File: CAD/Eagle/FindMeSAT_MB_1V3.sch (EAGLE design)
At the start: 136 parts, among them Q101 ABS07-32.768KHZ, Q651 ABM3B-16MHZ-10-R50-1-U, U1001 CFPT-141-20MHZ, U101 ATXMEGA256A3BU-AU, U1011 OPA354, U1021 OPA354, U1111 LM2831YMF, U1121 LM4120IM5-3.0, U201 SIM808, U301 MPU-9250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

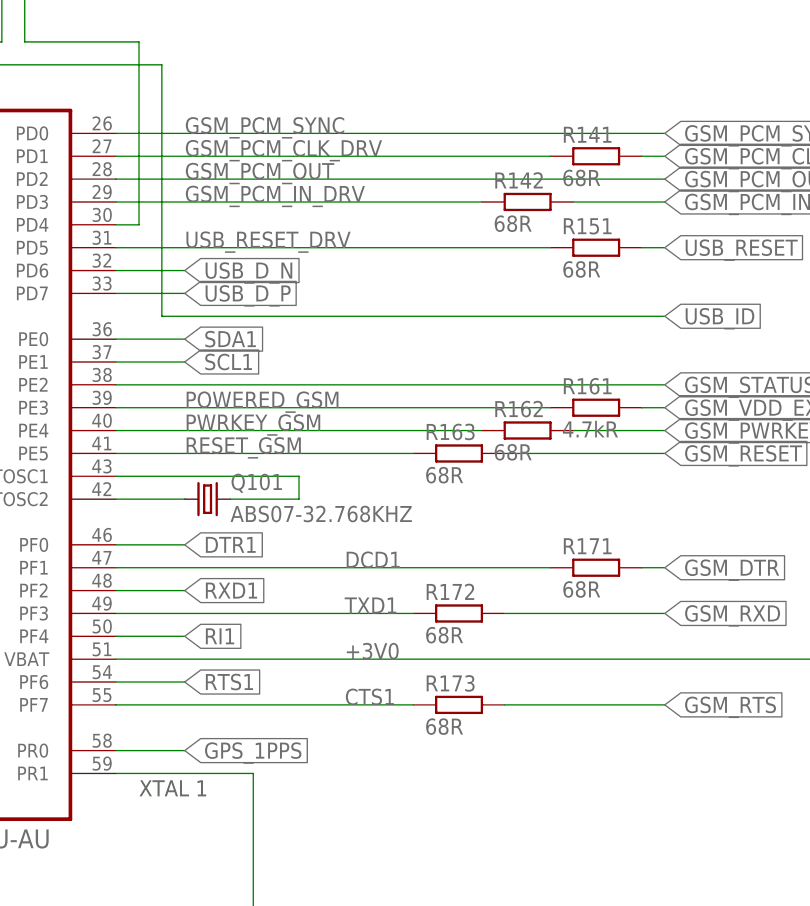
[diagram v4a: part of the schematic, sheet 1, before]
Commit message: HW_V1.3 - Polyfuse of USB - value changed from 0.5A/1.0A to 1.1A/2.2A - some net names fixed
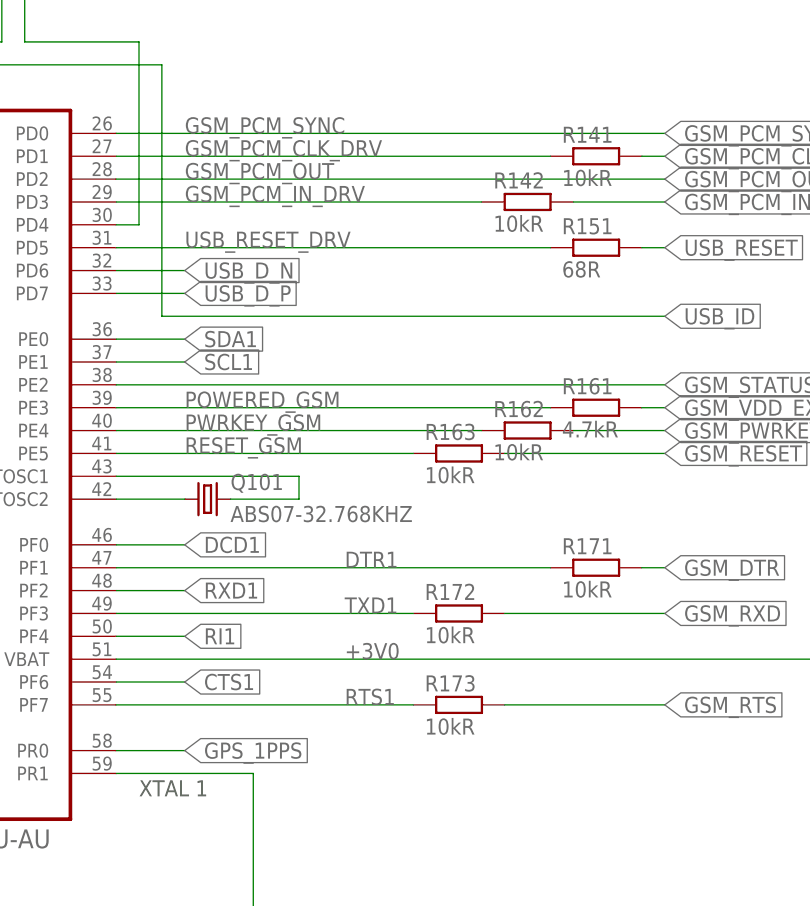
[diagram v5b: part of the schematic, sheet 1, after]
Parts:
- R141, R142, R162, R163, R171, R172, R173: value 68R -> 10kR
- RPOLY711: value 0.5A/1.0A -> 1.1A/2.2A
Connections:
- net CTS1: now also R223.1, U101A.PF6; no longer R173.1, U101A.PF7
- net DCD1: now also R222.1, U101A.PF0; no longer R171.1, U101A.PF1
- net DTR1: now also R171.1, U101A.PF1; no longer R222.1, U101A.PF0
- net RTS1: now also R173.1, U101A.PF7; no longer R223.1, U101A.PF6
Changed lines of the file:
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@@
 <part name="GND1203" library="df4iah_supply" deviceset="GND" device=""/>
 <part name="GND701" library="df4iah_supply" deviceset="GND" device=""/>
-<part name="RPOLY711" library="rcl" deviceset="R-EU_" device="M1206" value="0.5A/1.0A"/>
+<part name="RPOLY711" library="rcl" deviceset="R-EU_" device="M1206" value="1.1A/2.2A"/>
 <part name="R722" library="rcl" deviceset="R-EU_" device="R0603" value="68R"/>
 <part name="R723" library="rcl" deviceset="R-EU_" device="R0603" value="68R"/>
@@
 <part name="R212" library="rcl" deviceset="R-EU_" device="R0603" value="10kR"/>
 <part name="+3V3_211" library="df4iah_supply" deviceset="+3V3" device=""/>
-<part name="R172" library="rcl" deviceset="R-EU_" device="R0603" value="68R"/>
+<part name="R172" library="rcl" deviceset="R-EU_" device="R0603" value="10kR"/>
 <part name="R224" library="rcl" deviceset="R-EU_" device="R0603" value="68R"/>
 <part name="R223" library="rcl" deviceset="R-EU_" device="R0603" value="68R"/>
 <part name="R221" library="rcl" deviceset="R-EU_" device="R0603" value="68R"/>
-<part name="R173" library="rcl" deviceset="R-EU_" device="R0603" value="68R"/>
-<part name="R171" library="rcl" deviceset="R-EU_" device="R0603" value="68R"/>
+<part name="R173" library="rcl" deviceset="R-EU_" device="R0603" value="10kR"/>
+<part name="R171" library="rcl" deviceset="R-EU_" device="R0603" value="10kR"/>
 <part name="R222" library="rcl" deviceset="R-EU_" device="R0603" value="68R"/>
 <part name="R271" library="rcl" deviceset="R-EU_" device="R0805"/>
@@
 <part name="C251" library="rcl" deviceset="C-EU" device="C0603" value="100pF"/>
 <part name="GND231" library="df4iah_supply" deviceset="GND" device=""/>
-<part name="R163" library="rcl" deviceset="R-EU_" device="R0603" value="68R"/>
-<part name="R162" library="rcl" deviceset="R-EU_" device="R0603" value="68R"/>
+<part name="R163" library="rcl" deviceset="R-EU_" device="R0603" value="10kR"/>
+<part name="R162" library="rcl" deviceset="R-EU_" device="R0603" value="10kR"/>
 <part name="R161" library="rcl" deviceset="R-EU_" device="R0603" value="4.7kR"/>
 <part name="R231" library="rcl" deviceset="R-EU_" device="R0603" value="68R"/>
@@
 <part name="R234" library="rcl" deviceset="R-EU_" device="R0603" value="68R"/>
 <part name="R241" library="rcl" deviceset="R-EU_" device="R0603" value="68R"/>
-<part name="R141" library="rcl" deviceset="R-EU_" device="R0603" value="68R"/>
-<part name="R142" library="rcl" deviceset="R-EU_" device="R0603" value="68R"/>
+<part name="R141" library="rcl" deviceset="R-EU_" device="R0603" value="10kR"/>
+<part name="R142" library="rcl" deviceset="R-EU_" device="R0603" value="10kR"/>
 <part name="+3V3_121" library="df4iah_supply" deviceset="+3V3" device=""/>
 <part name="R251" library="rcl" deviceset="R-EU_" device="R0603" value="68R"/>
@@
 </segment>
 </net>
-<net name="RTS1" class="0">
+<net name="CTS1" class="0">
 <segment>
 <pinref part="U101" gate="A" pin="PF6"/>
@@
 </segment>
 </net>
-<net name="CTS1" class="0">
+<net name="RTS1" class="0">
 <segment>
 <pinref part="U101" gate="A" pin="PF7"/>
@@
 </segment>
 </net>
-<net name="DCD1" class="0">
+<net name="DTR1" class="0">
 <segment>
 <pinref part="R171" gate="G$1" pin="1"/>
@@
 </segment>
 </net>
-<net name="DTR1" class="0">
+<net name="DCD1" class="0">
 <segment>
 <pinref part="U101" gate="A" pin="PF0"/>
@@
 </segment>
 </net>
-<net name="RTS1" class="0">
-<segment>
-<pinref part="R223" gate="G$1" pin="1"/>
-<wire x1="86.36" y1="152.4" x2="33.02" y2="152.4" width="0.1524" layer="91"/>
-<label x="33.02" y="152.4" size="1.778" layer="95" rot="R180" xref="yes"/>
-</segment>
-</net>
 <net name="GSM_RI" class="0">
 <segment>
@@
 </segment>
 </net>
-<net name="DTR1" class="0">
+<net name="DCD1" class="0">
 <segment>
 <pinref part="R222" gate="G$1" pin="1"/>
@@
 </segment>
 </net>
+<net name="CTS1" class="0">
+<segment>
+<pinref part="R223" gate="G$1" pin="1"/>
+<wire x1="86.36" y1="152.4" x2="33.02" y2="152.4" width="0.1524" layer="91"/>
+<label x="33.02" y="152.4" size="1.778" layer="95" rot="R180" xref="yes"/>
+</segment>
+</net>

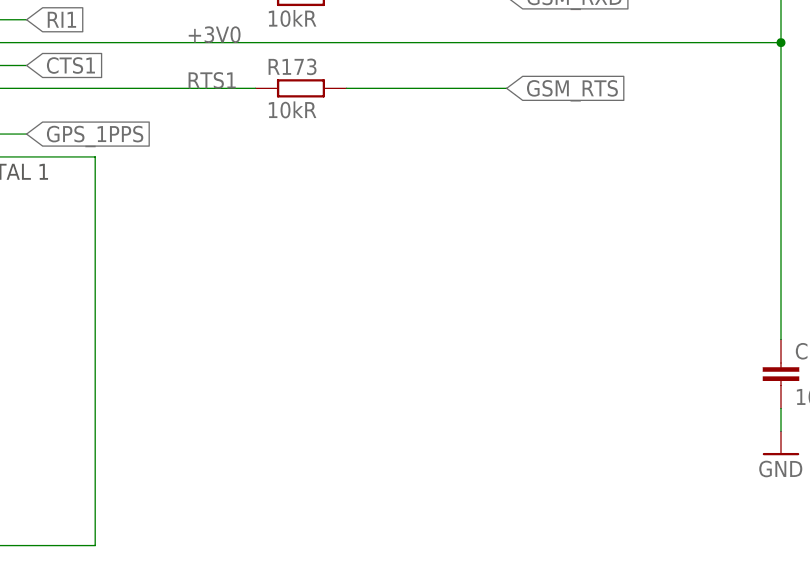
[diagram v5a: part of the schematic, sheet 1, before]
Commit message: HW_V1.3 - cable assignment for LCD-cable X-121 added
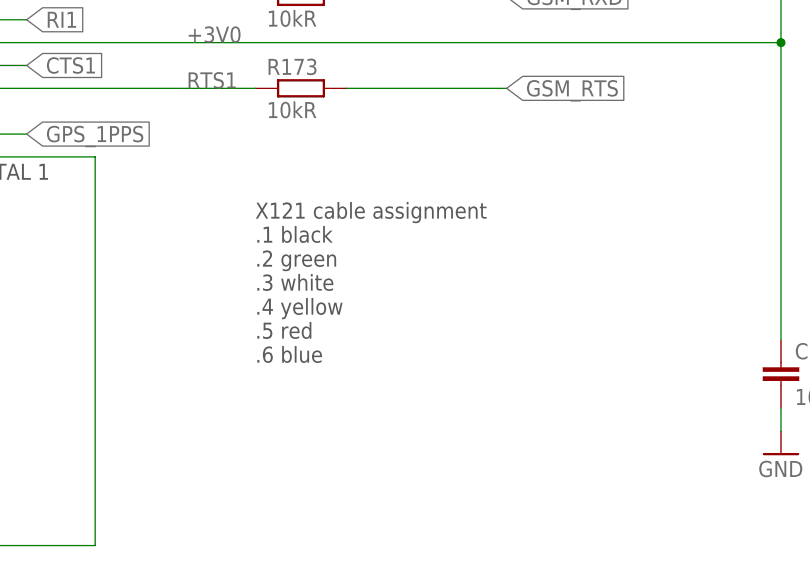
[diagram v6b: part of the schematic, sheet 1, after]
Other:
- note added: "X121 cable assignment .1 black .2 green .3 white .4 yellow .5 red .6 blue"
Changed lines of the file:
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@@
 <text x="39.624" y="70.612" size="1.778" layer="94" ratio="10">LCD</text>
 <text x="94.234" y="157.226" size="1.778" layer="94" ratio="10">I/O</text>
+<text x="162.56" y="45.72" size="1.778" layer="97">X121 cable assignment
+.1 black
+.2 green
+.3 white
+.4 yellow
+.5 red
+.6 blue</text>
 </plain>
 <instances>

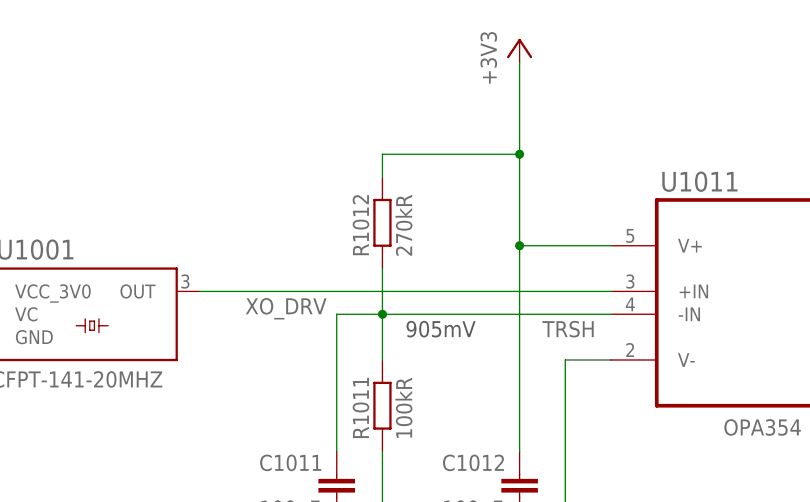
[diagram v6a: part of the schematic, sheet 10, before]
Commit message: HW_V1.3 - R1012: 270kR --> 330kR
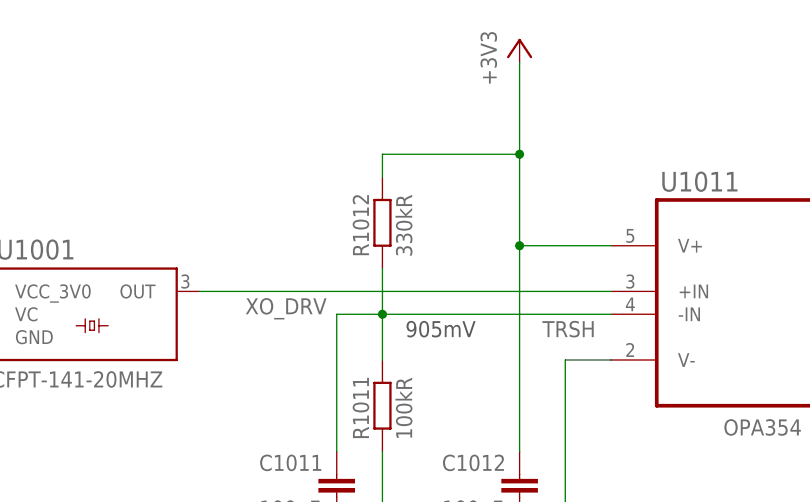
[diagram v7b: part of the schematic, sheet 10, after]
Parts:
- R1012: value 270kR -> 330kR
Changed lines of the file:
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@@
 <part name="C1012" library="rcl" deviceset="C-EU" device="C0603" value="100nF"/>
 <part name="+3V3_1011" library="df4iah_supply" deviceset="+3V3" device=""/>
-<part name="R1012" library="rcl" deviceset="R-EU_" device="R0603" value="270kR"/>
+<part name="R1012" library="rcl" deviceset="R-EU_" device="R0603" value="330kR"/>
 <part name="R1011" library="rcl" deviceset="R-EU_" device="R0603" value="100kR"/>
 <part name="GND1011" library="df4iah_supply" deviceset="GND" device=""/>

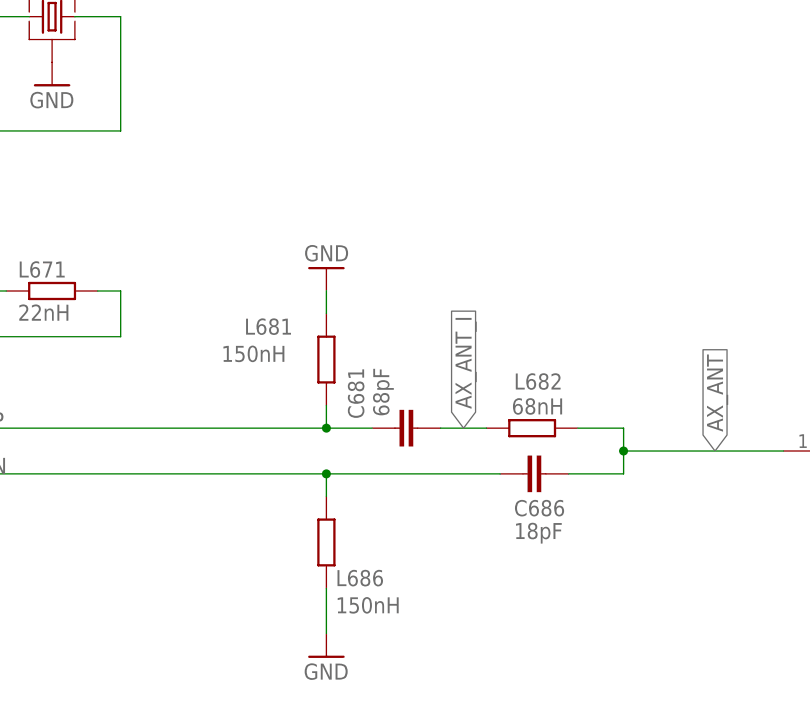
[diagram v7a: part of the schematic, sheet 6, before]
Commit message: HW_V1.3 - capacitor at VHF antenna added, miter applied
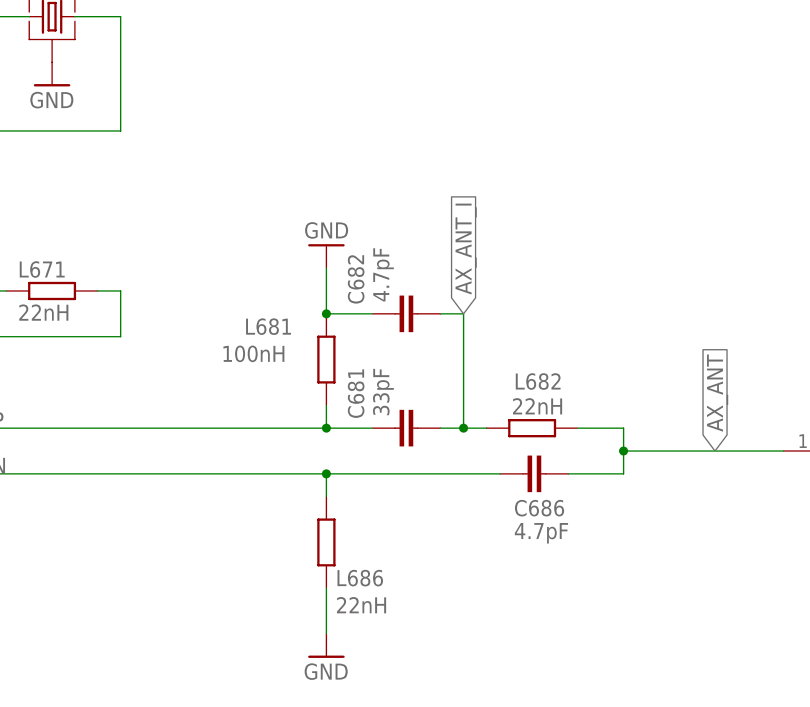
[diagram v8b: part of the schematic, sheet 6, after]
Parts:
- added C682: 4.7pF, rcl:C-EUC0603
- C681: value 68pF -> 33pF
- C686: value 18pF -> 4.7pF
- L681: value 150nH -> 100nH
- L682: value 68nH -> 22nH
- L686: value 150nH -> 22nH
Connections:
- net AX_ANT_I: now also C682.2
- net GND: now also C682.1
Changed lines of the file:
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@@
 <part name="Q651" library="df4iah_crystal" deviceset="ABM03B-16.000MHZ" device="" value="ABM3B-16MHZ-10-R50-1-U"/>
 <part name="L671" library="rcl" deviceset="R-EU_" device="R0603" value="22nH"/>
-<part name="C681" library="rcl" deviceset="C-EU" device="C0603" value="68pF"/>
+<part name="C681" library="rcl" deviceset="C-EU" device="C0603" value="33pF"/>
 <part name="GND683" library="df4iah_supply" deviceset="GND" device=""/>
-<part name="L686" library="rcl" deviceset="R-EU_" device="R0603" value="150nH"/>
-<part name="L682" library="rcl" deviceset="R-EU_" device="R0603" value="68nH"/>
+<part name="L686" library="rcl" deviceset="R-EU_" device="R0603" value="22nH"/>
+<part name="L682" library="rcl" deviceset="R-EU_" device="R0603" value="22nH"/>
 <part name="GND684" library="df4iah_supply" deviceset="GND" device=""/>
-<part name="C686" library="rcl" deviceset="C-EU" device="C0603" value="18pF"/>
-<part name="L681" library="rcl" deviceset="R-EU_" device="R0603" value="150nH"/>
+<part name="C686" library="rcl" deviceset="C-EU" device="C0603" value="4.7pF"/>
+<part name="L681" library="rcl" deviceset="R-EU_" device="R0603" value="100nH"/>
 <part name="X685" library="df4iah_connector" deviceset="SMA_SMT_AMPHENOL-901-143" device="" value="SMA_CON"/>
 <part name="GND689" library="df4iah_supply" deviceset="GND" device=""/>
@@
 <part name="C1141" library="rcl" deviceset="C-EU" device="C0603" value="100pF"/>
 <part name="C302" library="rcl" deviceset="C-EU" device="C0603" value="10nF"/>
+<part name="C682" library="rcl" deviceset="C-EU" device="C0603" value="4.7pF"/>
 </parts>
 <sheets>
@@
 <attribute name="VALUE" x="174.625" y="90.17" size="1.778" layer="96" rot="R90"/>
 </instance>
-<instance part="GND683" gate="1" x="167.64" y="106.68" rot="R180"/>
+<instance part="GND683" gate="1" x="167.64" y="109.22" rot="R180"/>
 <instance part="L686" gate="G$1" x="167.64" y="76.2" smashed="yes" rot="R90">
 <attribute name="NAME" x="168.656" y="71.3486" size="1.778" layer="95"/>
@@
 <instance part="GND689" gate="1" x="226.06" y="63.5"/>
 <instance part="GND651" gate="1" x="137.16" y="127"/>
+<instance part="C682" gate="G$1" x="175.26" y="101.6" smashed="yes" rot="R90">
+<attribute name="NAME" x="171.831" y="102.616" size="1.778" layer="95" rot="R90"/>
+<attribute name="VALUE" x="174.625" y="102.87" size="1.778" layer="96" rot="R90"/>
+</instance>
 </instances>
 <busses>
@@
 <pinref part="L681" gate="G$1" pin="2"/>
 <pinref part="GND683" gate="1" pin="GND"/>
-<wire x1="167.64" y1="104.14" x2="167.64" y2="101.6" width="0.1524" layer="91"/>
+<wire x1="167.64" y1="106.68" x2="167.64" y2="101.6" width="0.1524" layer="91"/>
+<pinref part="C682" gate="G$1" pin="1"/>
+<wire x1="167.64" y1="101.6" x2="172.72" y2="101.6" width="0.1524" layer="91"/>
+<junction x="167.64" y="101.6"/>
 </segment>
 <segment>
@@
 <pinref part="C681" gate="G$1" pin="2"/>
 <pinref part="L682" gate="G$1" pin="1"/>
-<wire x1="180.34" y1="88.9" x2="185.42" y2="88.9" width="0.1524" layer="91"/>
-<label x="182.88" y="88.9" size="1.778" layer="95" rot="R90" xref="yes"/>
-</segment>
-</net>
+<wire x1="180.34" y1="88.9" x2="182.88" y2="88.9" width="0.1524" layer="91"/>
+<pinref part="C682" gate="G$1" pin="2"/>
+<wire x1="182.88" y1="88.9" x2="185.42" y2="88.9" width="0.1524" layer="91"/>
+<wire x1="182.88" y1="88.9" x2="182.88" y2="101.6" width="0.1524" layer="91"/>
+<wire x1="182.88" y1="101.6" x2="180.34" y2="101.6" width="0.1524" layer="91"/>
+<junction x="182.88" y="88.9"/>
+<label x="182.88" y="101.6" size="1.778" layer="95" rot="R90" xref="yes"/>
+</segment>
+</net>
